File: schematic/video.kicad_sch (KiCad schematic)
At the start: 9 parts, among them U10 MK4116P, U11 MK4116P, U12 MK4116P, U13 MK4116P, U14 MK4116P, U15 MK4116P, U16 MK4116P, U17 MK4116P, U9 TMS9928A

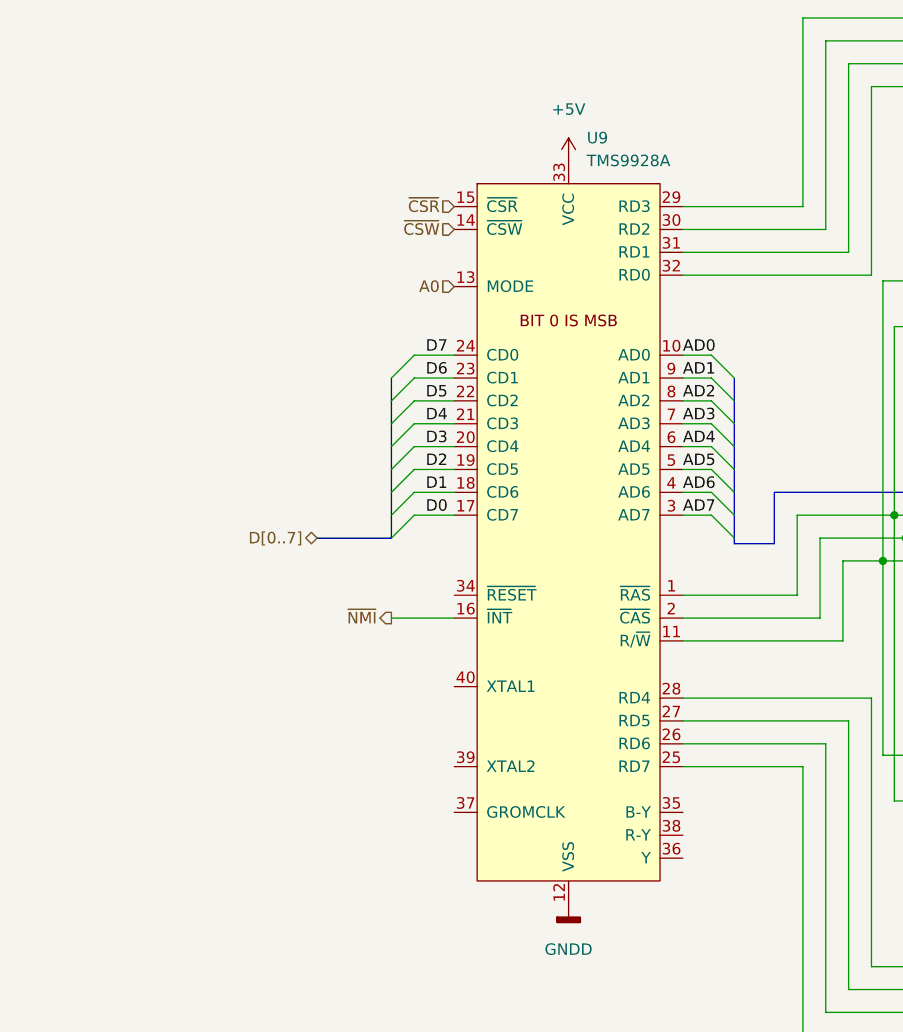
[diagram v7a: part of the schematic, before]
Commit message: completed sound block, finished cart io port, and finished decoder.
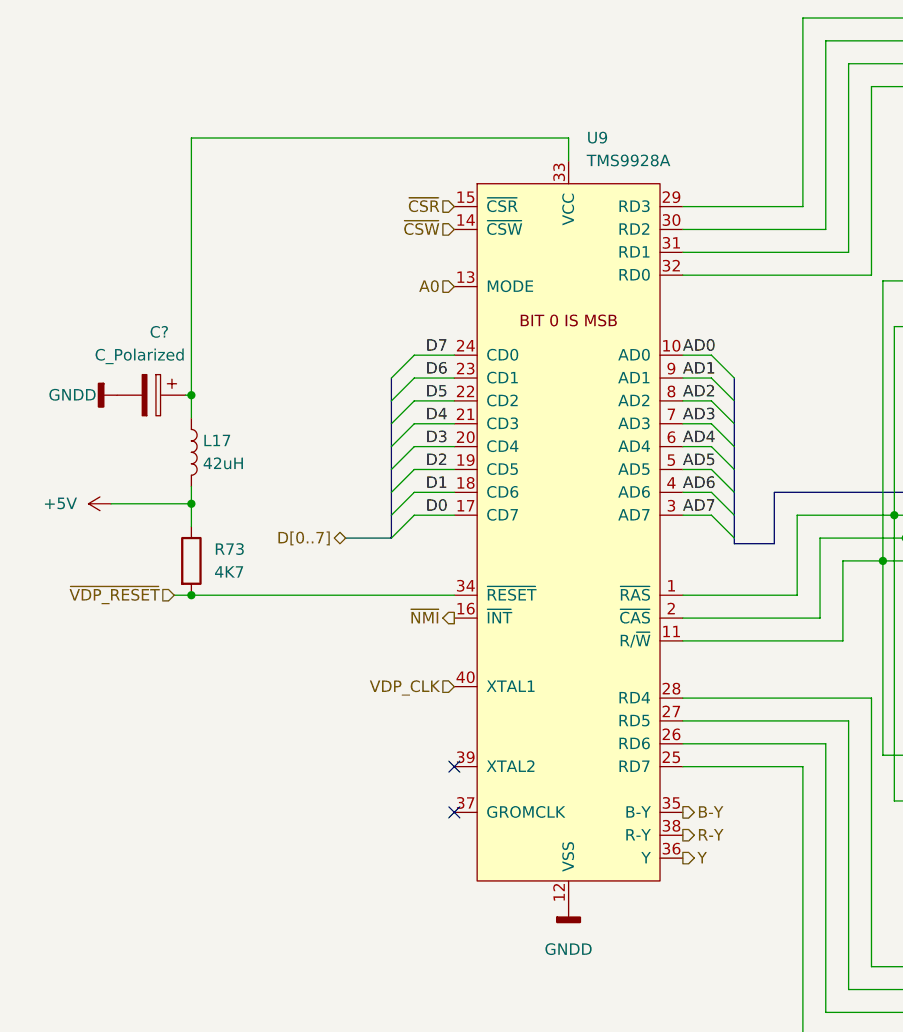
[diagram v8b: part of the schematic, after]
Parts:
- added C?: C_Polarized, symbol Device:C_Polarized
- added L17: 42uH, symbol Device:L
- added R73: 4K7, symbol Device:R
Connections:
- net +5V: now also L17.2, R73.1; no longer U9.33 (VCC)
- net GNDD: now also C?.2
- net ~{VDP_RESET}: now reaches U9.34 (~{RESET})
- net ~{VDP_RESET}: now also R73.2
- net B-Y: now reaches U9.35 (B-Y)
- net Y: now reaches U9.36 (Y)
- net R-Y: now reaches U9.38 (R-Y)
- net VDP_CLK: now reaches U9.40 (XTAL1)
- new net: C?.1, L17.1, U9.33 (VCC)
- no-connect marks 0 -> 2
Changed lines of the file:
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@@
 (kicad_sch (version 20211123) (generator eeschema)
   (paper "A4")
+  (junction (at 34.29 91.44) (diameter 0) (color 0 0 0 0)
+  )
   (junction (at 172.085 80.01) (diameter 0) (color 0 0 0 0)
   )
@@
   (junction (at 112.395 82.55) (diameter 0) (color 0 0 0 0)
   )
+  (junction (at 34.29 69.215) (diameter 0) (color 0 0 0 0)
+  )
   (junction (at 174.625 87.63) (diameter 0) (color 0 0 0 0)
   )
+  (junction (at 34.29 81.28) (diameter 0) (color 0 0 0 0)
+  )
   (junction (at 175.895 82.55) (diameter 0) (color 0 0 0 0)
   )
@@
   (junction (at 177.165 85.09) (diameter 0) (color 0 0 0 0)
   )
+  (no_connect (at 63.5 110.49))
+  (no_connect (at 63.5 115.57))
   (bus_entry (at 137.795 104.14) (size 2.54 2.54)
     (stroke (width 0) (type default) (color 0 0 0 0))
@@
     (stroke (width 0) (type default) (color 0 0 0 0))
   )
+  (wire (pts (xy 34.29 81.28) (xy 34.29 83.82))
+    (stroke (width 0) (type default) (color 0 0 0 0))
+  )
   (bus (pts (xy 140.335 71.755) (xy 140.335 80.01))
     (stroke (width 0) (type default) (color 0 0 0 0))
@@
     (stroke (width 0) (type default) (color 0 0 0 0))
   )
+  (wire (pts (xy 76.2 40.64) (xy 76.2 43.18))
+    (stroke (width 0) (type default) (color 0 0 0 0))
+  )
   (wire (pts (xy 59.055 67.31) (xy 63.5 67.31))
     (stroke (width 0) (type default) (color 0 0 0 0))
@@
     (stroke (width 0) (type default) (color 0 0 0 0))
   )
+  (wire (pts (xy 34.29 69.215) (xy 34.29 40.64))
+    (stroke (width 0) (type default) (color 0 0 0 0))
+  )
   (wire (pts (xy 104.14 85.09) (xy 104.14 93.98))
     (stroke (width 0) (type default) (color 0 0 0 0))
@@
     (stroke (width 0) (type default) (color 0 0 0 0))
   )
-  (bus (pts (xy 56.515 85.09) (xy 48.26 85.09))
+  (bus (pts (xy 56.515 85.09) (xy 51.435 85.09))
     (stroke (width 0) (type default) (color 0 0 0 0))
   )
@@
     (stroke (width 0) (type default) (color 0 0 0 0))
   )
+  (wire (pts (xy 32.385 91.44) (xy 34.29 91.44))
+    (stroke (width 0) (type default) (color 0 0 0 0))
+  )
   (bus (pts (xy 172.085 114.3) (xy 172.085 116.84))
     (stroke (width 0) (type default) (color 0 0 0 0))
@@
     (stroke (width 0) (type default) (color 0 0 0 0))
   )
+  (wire (pts (xy 34.29 91.44) (xy 63.5 91.44))
+    (stroke (width 0) (type default) (color 0 0 0 0))
+  )
   (bus (pts (xy 140.335 109.22) (xy 140.335 111.76))
     (stroke (width 0) (type default) (color 0 0 0 0))
@@
     (stroke (width 0) (type default) (color 0 0 0 0))
   )
+  (wire (pts (xy 34.29 69.215) (xy 33.655 69.215))
+    (stroke (width 0) (type default) (color 0 0 0 0))
+  )
   (wire (pts (xy 107.315 135.255) (xy 173.355 135.255))
     (stroke (width 0) (type default) (color 0 0 0 0))
@@
     (stroke (width 0) (type default) (color 0 0 0 0))
   )
+  (wire (pts (xy 34.29 40.64) (xy 76.2 40.64))
+    (stroke (width 0) (type default) (color 0 0 0 0))
+  )
   (wire (pts (xy 142.875 87.63) (xy 174.625 87.63))
     (stroke (width 0) (type default) (color 0 0 0 0))
@@
     (stroke (width 0) (type default) (color 0 0 0 0))
   )
+  (wire (pts (xy 34.29 79.375) (xy 34.29 81.28))
+    (stroke (width 0) (type default) (color 0 0 0 0))
+  )
   (bus (pts (xy 172.085 71.755) (xy 172.085 80.01))
     (stroke (width 0) (type default) (color 0 0 0 0))
@@
     (stroke (width 0) (type default) (color 0 0 0 0))
   )
+  (wire (pts (xy 25.4 81.28) (xy 34.29 81.28))
+    (stroke (width 0) (type default) (color 0 0 0 0))
+  )
   (wire (pts (xy 178.435 109.22) (xy 174.625 109.22))
     (stroke (width 0) (type default) (color 0 0 0 0))
@@
     (stroke (width 0) (type default) (color 0 0 0 0))
   )
-  (wire (pts (xy 56.515 93.98) (xy 63.5 93.98))
-    (stroke (width 0) (type default) (color 0 0 0 0))
-  )
   (wire (pts (xy 167.005 51.435) (xy 169.545 51.435))
     (stroke (width 0) (type default) (color 0 0 0 0))
@@
     (stroke (width 0) (type default) (color 0 0 0 0))
   )
+  (wire (pts (xy 34.29 71.755) (xy 34.29 69.215))
+    (stroke (width 0) (type default) (color 0 0 0 0))
+  )
   (wire (pts (xy 230.505 114.3) (xy 233.045 114.3))
     (stroke (width 0) (type default) (color 0 0 0 0))
@@
   (label "AD6" (at 135.255 48.895 0)
     (effects (font (size 1.27 1.27)) (justify left bottom))
+  )
+  (hierarchical_label "Y" (shape output) (at 88.9 120.65 0)
+    (effects (font (size 1.27 1.27)) (justify left))
   )
   (hierarchical_label "~{CSW}" (shape input) (at 63.5 50.8 180)
     (effects (font (size 1.27 1.27)) (justify right))
   )
-  (hierarchical_label "D[0..7]" (shape bidirectional) (at 48.26 85.09 180)
+  (hierarchical_label "D[0..7]" (shape bidirectional) (at 51.435 85.09 180)
     (effects (font (size 1.27 1.27)) (justify right))
+  )
+  (hierarchical_label "R-Y" (shape output) (at 88.9 118.11 0)
+    (effects (font (size 1.27 1.27)) (justify left))
   )
   (hierarchical_label "~{CSR}" (shape input) (at 63.5 48.26 180)
     (effects (font (size 1.27 1.27)) (justify right))
   )
-  (hierarchical_label "~{NMI}" (shape output) (at 56.515 93.98 180)
+  (hierarchical_label "~{VDP_RESET}" (shape input) (at 32.385 91.44 180)
     (effects (font (size 1.27 1.27)) (justify right))
   )
+  (hierarchical_label "~{NMI}" (shape output) (at 63.5 93.98 180)
+    (effects (font (size 1.27 1.27)) (justify right))
+  )
   (hierarchical_label "A0" (shape input) (at 63.5 57.15 180)
+    (effects (font (size 1.27 1.27)) (justify right))
+  )
+  (hierarchical_label "B-Y" (shape output) (at 88.9 115.57 0)
+    (effects (font (size 1.27 1.27)) (justify left))
+  )
+  (hierarchical_label "VDP_CLK" (shape input) (at 63.5 101.6 180)
     (effects (font (size 1.27 1.27)) (justify right))
   )
@@
     (pin "1")
   )
+  (symbol (lib_id "Device:L") (at 34.29 75.565 0) (unit 1)
+    (in_bom yes) (on_board yes) (fields_autoplaced)
+    (property "Reference" "L17" (id 0) (at 35.56 74.2949 0)
+      (effects (font (size 1.27 1.27)) (justify left))
+    )
+    (property "Value" "42uH" (id 1) (at 35.56 76.8349 0)
+      (effects (font (size 1.27 1.27)) (justify left))
+    )
+    (property "Footprint" "" (id 2) (at 34.29 75.565 0)
+      (effects (font (size 1.27 1.27)) hide)
+    )
+    (property "Datasheet" "~" (id 3) (at 34.29 75.565 0)
+      (effects (font (size 1.27 1.27)) hide)
+    )
+    (pin "1")
+    (pin "2")
+  )
   (symbol (lib_id "power:+5V") (at 188.595 93.98 0) (unit 1)
     (in_bom yes) (on_board yes)
@@
     (pin "8")
     (pin "9")
-  )
-  (symbol (lib_id "power:+5V") (at 76.2 43.18 0) (unit 1)
-    (in_bom yes) (on_board yes) (fields_autoplaced)
-    (property "Reference" "#PWR?" (id 0) (at 76.2 46.99 0)
-      (effects (font (size 1.27 1.27)) hide)
-    )
-    (property "Value" "+5V" (id 1) (at 76.2 37.465 0))
-    (property "Footprint" "" (id 2) (at 76.2 43.18 0)
-      (effects (font (size 1.27 1.27)) hide)
-    )
-    (property "Datasheet" "" (id 3) (at 76.2 43.18 0)
-      (effects (font (size 1.27 1.27)) hide)
-    )
-    (pin "1")
   )
   (symbol (lib_id "power:+5V") (at 188.595 41.275 0) (unit 1)
@@
     (pin "1")
   )
+  (symbol (lib_id "power:+5V") (at 25.4 81.28 90) (unit 1)
+    (in_bom yes) (on_board yes) (fields_autoplaced)
+    (property "Reference" "#PWR?" (id 0) (at 29.21 81.28 0)
+      (effects (font (size 1.27 1.27)) hide)
+    )
+    (property "Value" "+5V" (id 1) (at 21.59 81.2799 90)
+      (effects (font (size 1.27 1.27)) (justify left))
+    )
+    (property "Footprint" "" (id 2) (at 25.4 81.28 0)
+      (effects (font (size 1.27 1.27)) hide)
+    )
+    (property "Datasheet" "" (id 3) (at 25.4 81.28 0)
+      (effects (font (size 1.27 1.27)) hide)
+    )
+    (pin "1")
+  )
   (symbol (lib_id "power:+5V") (at 125.095 41.275 0) (unit 1)
     (in_bom yes) (on_board yes)
@@
     (pin "1")
   )
+  (symbol (lib_id "power:GNDD") (at 26.035 69.215 270) (unit 1)
+    (in_bom yes) (on_board yes)
+    (property "Reference" "#PWR?" (id 0) (at 19.685 69.215 0)
+      (effects (font (size 1.27 1.27)) hide)
+    )
+    (property "Value" "GNDD" (id 1) (at 18.415 69.215 90)
+      (effects (font (size 1.27 1.27)) (justify left))
+    )
+    (property "Footprint" "" (id 2) (at 26.035 69.215 0)
+      (effects (font (size 1.27 1.27)) hide)
+    )
+    (property "Datasheet" "" (id 3) (at 26.035 69.215 0)
+      (effects (font (size 1.27 1.27)) hide)
+    )
+    (pin "1")
+  )
   (symbol (lib_id "power:-5V") (at 217.805 41.275 0) (unit 1)
     (in_bom yes) (on_board yes) (fields_autoplaced)
@@
     )
     (pin "1")
+  )
+  (symbol (lib_id "Device:C_Polarized") (at 29.845 69.215 270) (unit 1)
+    (in_bom yes) (on_board yes)
+    (property "Reference" "C?" (id 0) (at 30.734 62.23 90))
+    (property "Value" "C_Polarized" (id 1) (at 28.575 64.77 90))
+    (property "Footprint" "" (id 2) (at 26.035 70.1802 0)
+      (effects (font (size 1.27 1.27)) hide)
+    )
+    (property "Datasheet" "~" (id 3) (at 29.845 69.215 0)
+      (effects (font (size 1.27 1.27)) hide)
+    )
+    (pin "1")
+    (pin "2")
   )
   (symbol (lib_id "power:+12V") (at 151.765 93.98 0) (unit 1)
@@
     (pin "9")
   )
+  (symbol (lib_id "Device:R") (at 34.29 87.63 0) (unit 1)
+    (in_bom yes) (on_board yes) (fields_autoplaced)
+    (property "Reference" "R73" (id 0) (at 36.83 86.3599 0)
+      (effects (font (size 1.27 1.27)) (justify left))
+    )
+    (property "Value" "4K7" (id 1) (at 36.83 88.8999 0)
+      (effects (font (size 1.27 1.27)) (justify left))
+    )
+    (property "Footprint" "" (id 2) (at 32.512 87.63 90)
+      (effects (font (size 1.27 1.27)) hide)
+    )
+    (property "Datasheet" "~" (id 3) (at 34.29 87.63 0)
+      (effects (font (size 1.27 1.27)) hide)
+    )
+    (pin "1")
+    (pin "2")
+  )
   (symbol (lib_id "power:GNDD") (at 220.345 125.73 0) (unit 1)
